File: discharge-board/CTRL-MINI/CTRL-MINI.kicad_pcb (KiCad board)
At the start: 2 copper layers, 119.4 x 71.1 mm, 17 parts, among them J1 Conn_01x04_Pin, J10 Conn_01x04_Pin, J11 MD2-L, J12 MD2-R, J13 Conn_01x08_Pin, J2 MD0-L, J3 MD0-R, J4 Screw_Terminal_01x02, J5 Conn_01x04_Pin, J6 MD1-L, J7 MD1-R, J8 RPP-L, J9 RPP-R, U1 BD50FC0FP

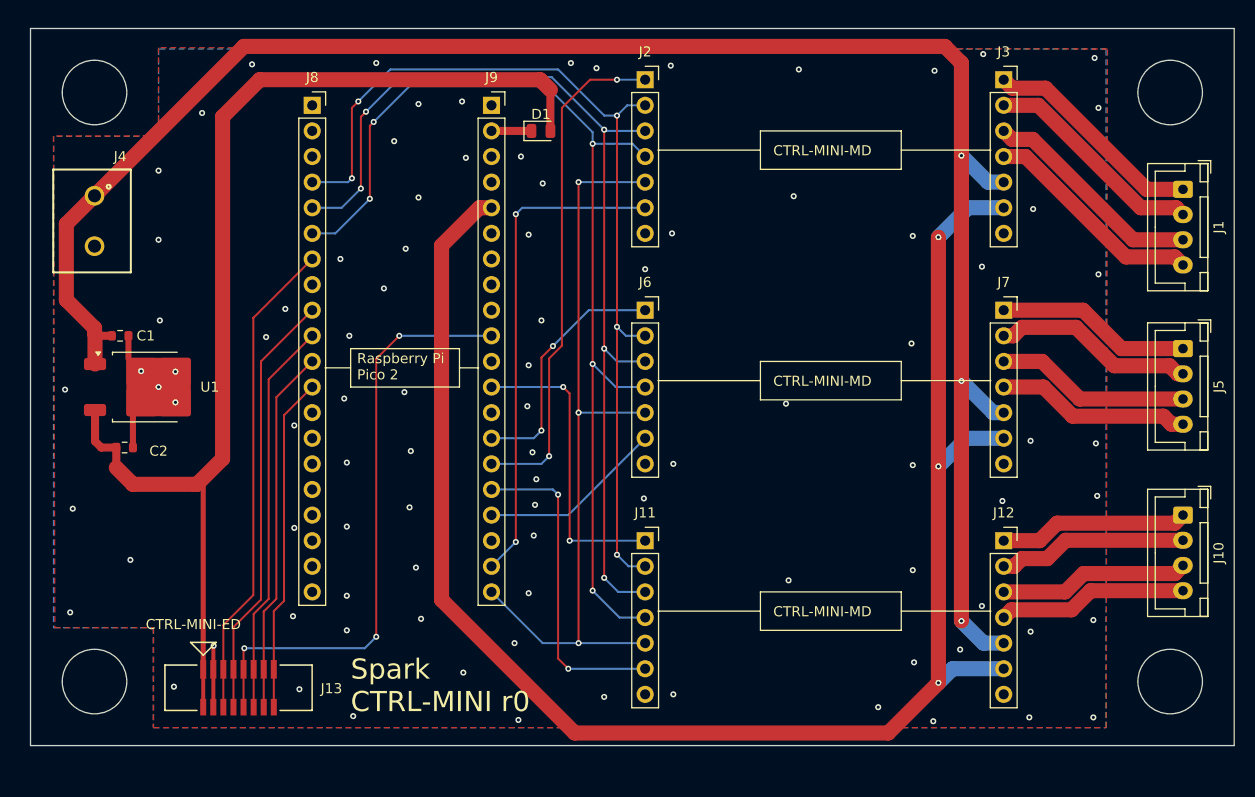
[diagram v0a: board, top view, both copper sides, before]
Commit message: Change CTRl-MINI MB size to metric
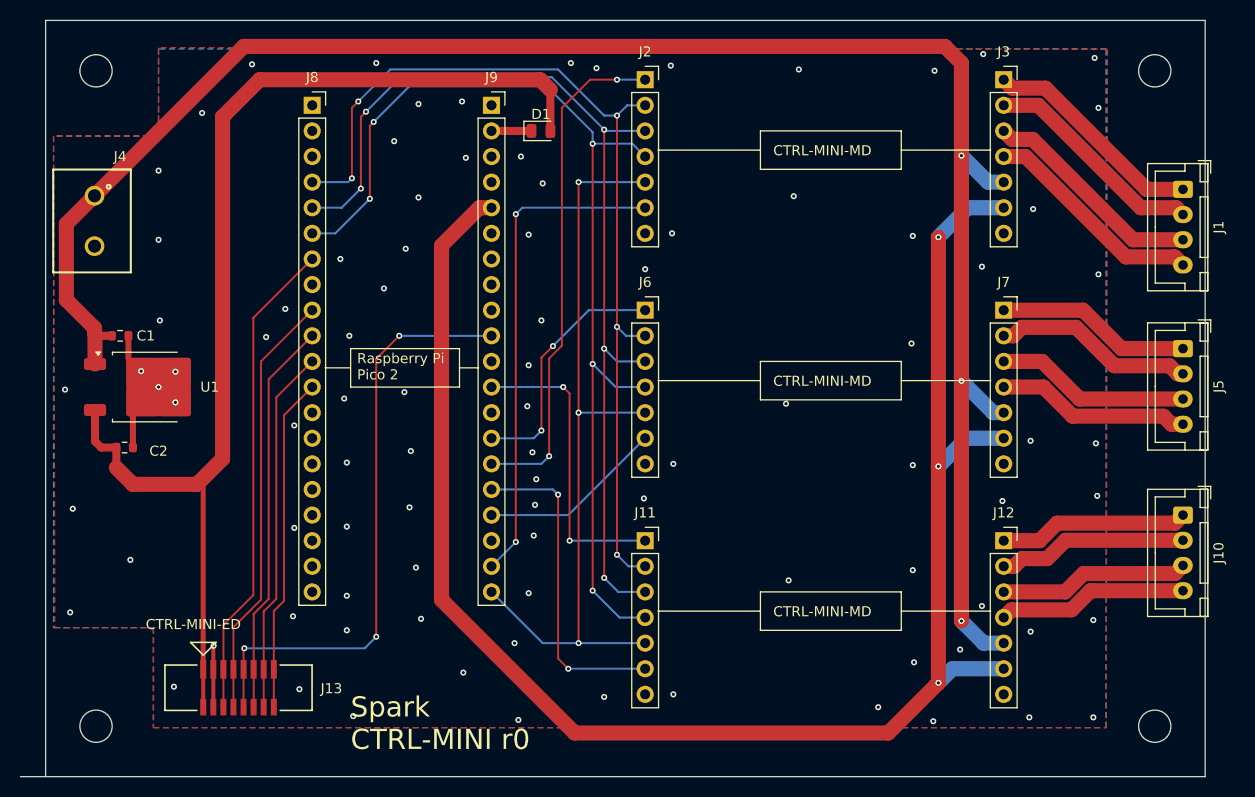
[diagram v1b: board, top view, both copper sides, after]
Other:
- board size 119.4 x 71.1 mm -> 117.5 x 75 mm

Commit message: Increase silkscreen width & avoid via-silk collision
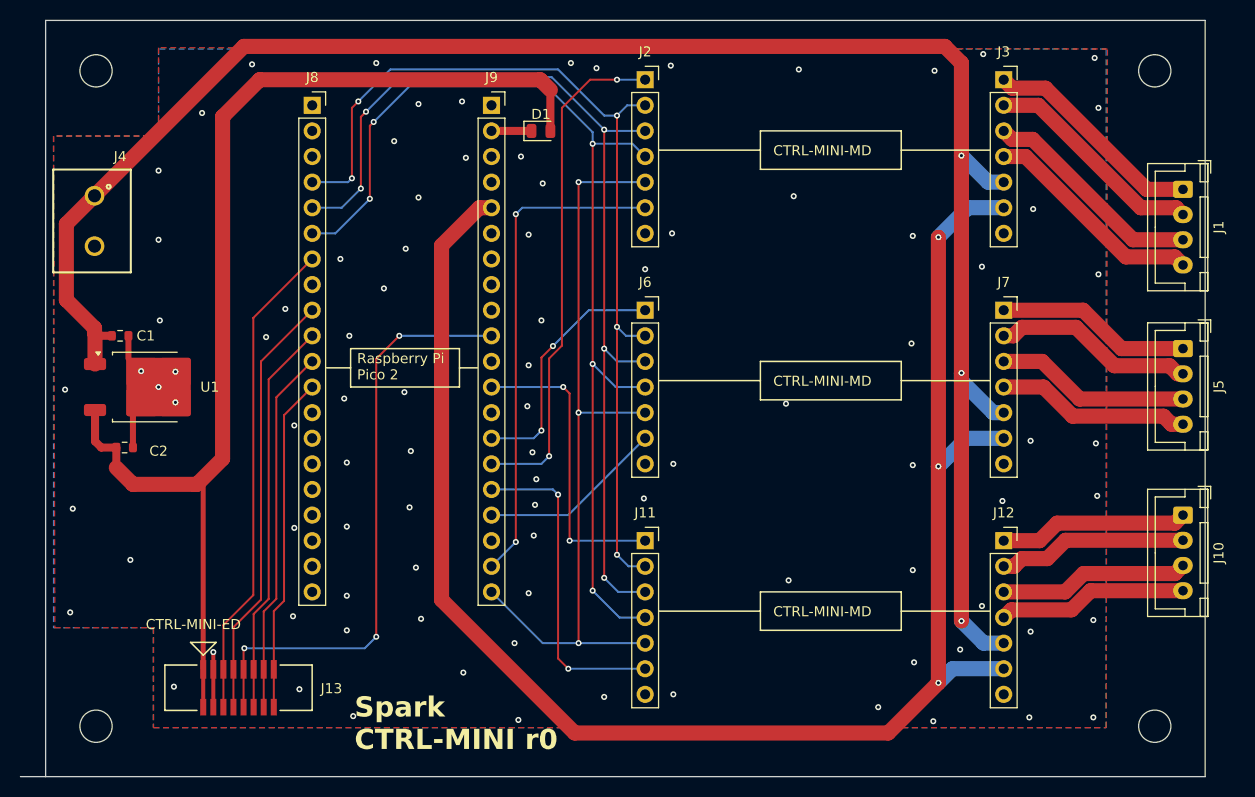
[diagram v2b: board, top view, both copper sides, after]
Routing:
- net +12V: track 184.8 -> 185.6 mm
- net GND: track 15.0 -> 14.4 mm
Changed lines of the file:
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@@
 	(gr_line
 		(start 106.045 84.455)
-		(end 107.95 84.455)
-		(stroke
-			(width 0.1)
+		(end 107.823 84.455)
+		(stroke
+			(width 0.15)
 			(type default)
 		)
@@
 	(gr_line
 		(start 149.86 108.585)
-		(end 158.75 108.585)
-		(stroke
-			(width 0.1)
+		(end 158.623 108.585)
+		(stroke
+			(width 0.15)
 			(type default)
 		)
@@
 		(end 149.86 106.68)
 		(stroke
-			(width 0.1)
+			(width 0.15)
 			(type default)
 		)
@@
 		(end 149.86 60.96)
 		(stroke
-			(width 0.1)
+			(width 0.15)
 			(type default)
 		)
@@
 		(end 135.89 110.49)
 		(stroke
-			(width 0.1)
+			(width 0.15)
 			(type default)
 		)
@@
 		(end 135.89 64.77)
 		(stroke
-			(width 0.1)
+			(width 0.15)
 			(type default)
 		)
@@
 	(gr_line
 		(start 135.89 85.725)
-		(end 125.73 85.725)
-		(stroke
-			(width 0.1)
+		(end 125.857 85.725)
+		(stroke
+			(width 0.15)
 			(type default)
 		)
@@
 		(end 135.89 60.96)
 		(stroke
-			(width 0.1)
+			(width 0.15)
 			(type default)
 		)
@@
 	(gr_line
 		(start 95.25 84.455)
-		(end 92.71 84.455)
-		(stroke
-			(width 0.1)
+		(end 92.837 84.455)
+		(stroke
+			(width 0.15)
 			(type default)
 		)
@@
 		(end 149.86 64.77)
 		(stroke
-			(width 0.1)
+			(width 0.15)
 			(type default)
 		)
@@
 	(gr_line
 		(start 135.89 62.865)
-		(end 125.73 62.865)
-		(stroke
-			(width 0.1)
+		(end 125.857 62.865)
+		(stroke
+			(width 0.15)
 			(type default)
 		)
@@
 		(end 149.86 83.82)
 		(stroke
-			(width 0.1)
+			(width 0.15)
 			(type default)
 		)
@@
 		(end 95.25 82.55)
 		(stroke
-			(width 0.1)
+			(width 0.15)
 			(type default)
 		)
@@
 		(end 149.86 110.49)
 		(stroke
-			(width 0.1)
+			(width 0.15)
 			(type default)
 		)
@@
 		(end 106.045 86.36)
 		(stroke
-			(width 0.1)
+			(width 0.15)
 			(type default)
 		)
@@
 		(end 135.89 87.63)
 		(stroke
-			(width 0.1)
+			(width 0.15)
 			(type default)
 		)
@@
 		(end 95.25 86.36)
 		(stroke
-			(width 0.1)
+			(width 0.15)
 			(type default)
 		)
@@
 		(end 135.89 83.82)
 		(stroke
-			(width 0.1)
+			(width 0.15)
 			(type default)
 		)
@@
 		(end 135.89 106.68)
 		(stroke
-			(width 0.1)
+			(width 0.15)
 			(type default)
 		)
@@
 		(end 149.86 87.63)
 		(stroke
-			(width 0.1)
+			(width 0.15)
 			(type default)
 		)
@@
 	(gr_line
 		(start 149.86 62.865)
-		(end 158.75 62.865)
-		(stroke
-			(width 0.1)
+		(end 158.623 62.865)
+		(stroke
+			(width 0.15)
 			(type default)
 		)
@@
 	(gr_line
 		(start 135.89 108.585)
-		(end 125.73 108.585)
-		(stroke
-			(width 0.1)
+		(end 125.857 108.585)
+		(stroke
+			(width 0.15)
 			(type default)
 		)
@@
 		(end 106.045 82.55)
 		(stroke
-			(width 0.1)
+			(width 0.15)
 			(type default)
 		)
@@
 	(gr_line
 		(start 149.86 85.725)
-		(end 158.75 85.725)
-		(stroke
-			(width 0.1)
+		(end 158.623 85.725)
+		(stroke
+			(width 0.15)
 			(type default)
 		)
@@
 			(font
 				(size 1 1)
-				(thickness 0.1)
+				(thickness 0.15)
 			)
 			(justify left bottom)
@@
 	)
 	(gr_text "Spark\nCTRL-MINI r0"
-		(at 95.25 122.5 0)
+		(at 95.631 122.5 0)
 		(layer "F.SilkS")
 		(effects
 			(font
 				(size 2 2)
-				(thickness 0.2)
+				(thickness 0.4)
+				(bold yes)
 			)
 			(justify left bottom)
@@
 			(font
 				(size 1 1)
-				(thickness 0.1)
+				(thickness 0.15)
 			)
 			(justify left bottom)
@@
 			(font
 				(size 1 1)
-				(thickness 0.1)
+				(thickness 0.15)
 			)
 			(justify left bottom)
@@
 			(font
 				(size 1 1)
-				(thickness 0.1)
+				(thickness 0.15)
 			)
 			(justify left bottom)
@@
 			(font
 				(size 1 1)
-				(thickness 0.1)
+				(thickness 0.15)
 			)
 			(justify left bottom)
@@
 	)
 	(segment
+		(start 81.63 112.649)
+		(end 81.63 114.36)
+		(width 0.4)
+		(layer "F.Cu")
+		(net 1)
+	)
+	(segment
 		(start 73.66 92.36)
 		(end 73.66 88.75)
@@
 	)
 	(segment
-		(start 81.661 112.014)
-		(end 81.63 112.045)
-		(width 0.4)
-		(layer "F.Cu")
-		(net 1)
-	)
-	(segment
 		(start 73.215 83.525)
 		(end 74.474 84.784)
@@
 		(net 1)
 	)
-	(segment
-		(start 81.63 112.045)
-		(end 81.63 114.36)
-		(width 0.4)
-		(layer "F.Cu")
-		(net 1)
-	)
 	(via
 		(at 100.584 86.868)
@@
 	)
 	(via
-		(at 81.661 112.014)
+		(at 81.63 112.649)
 		(size 0.6)
 		(drill 0.3)
@@
 	)
 	(segment
+		(start 155.829 84.963)
+		(end 155.829 63.406959)
+		(width 1.5)
+		(layer "F.Cu")
+		(net 2)
+	)
+	(segment
 		(start 67.056 70.184)
 		(end 67.056 77.724)
@@
 	(segment
 		(start 155.829 109.56704)
-		(end 155.829 85.758959)
+		(end 155.829 84.963)
 		(width 1.5)
 		(layer "F.Cu")
@@
 	)
 	(segment
-		(start 155.829 85.758959)
-		(end 155.829 63.406959)
-		(width 1.5)
-		(layer "F.Cu")
-		(net 2)
-	)
-	(segment
 		(start 69.85 67.39)
 		(end 67.056 70.184)
@@
 	)
 	(via
-		(at 155.829 85.758959)
+		(at 155.829 84.963)
 		(size 0.6)
 		(drill 0.3)
@@
 	(segment
 		(start 158.970041 88.9)
-		(end 155.829 85.758959)
-		(width 1.5)
-		(layer "B.Cu")
-		(net 2)
-	)
-	(segment
-		(start 160.02 88.9)
-		(end 158.970041 88.9)
+		(end 160.02 88.9)
 		(width 1.5)
 		(layer "B.Cu")
@@
 		(width 1.5)
 		(layer "B.Cu")
+		(net 2)
+	)
+	(segment
+		(start 155.829 84.963)
+		(end 155.829 85.758959)
+		(width 1.5)
+		(layer "B.Cu")
+		(net 2)
+	)
+	(segment
+		(start 155.829 85.758959)
+		(end 158.970041 88.9)
+		(width 1.5)
+		(layer "B.Cu")

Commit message: Improve manufacturability of MB, use SOD-523
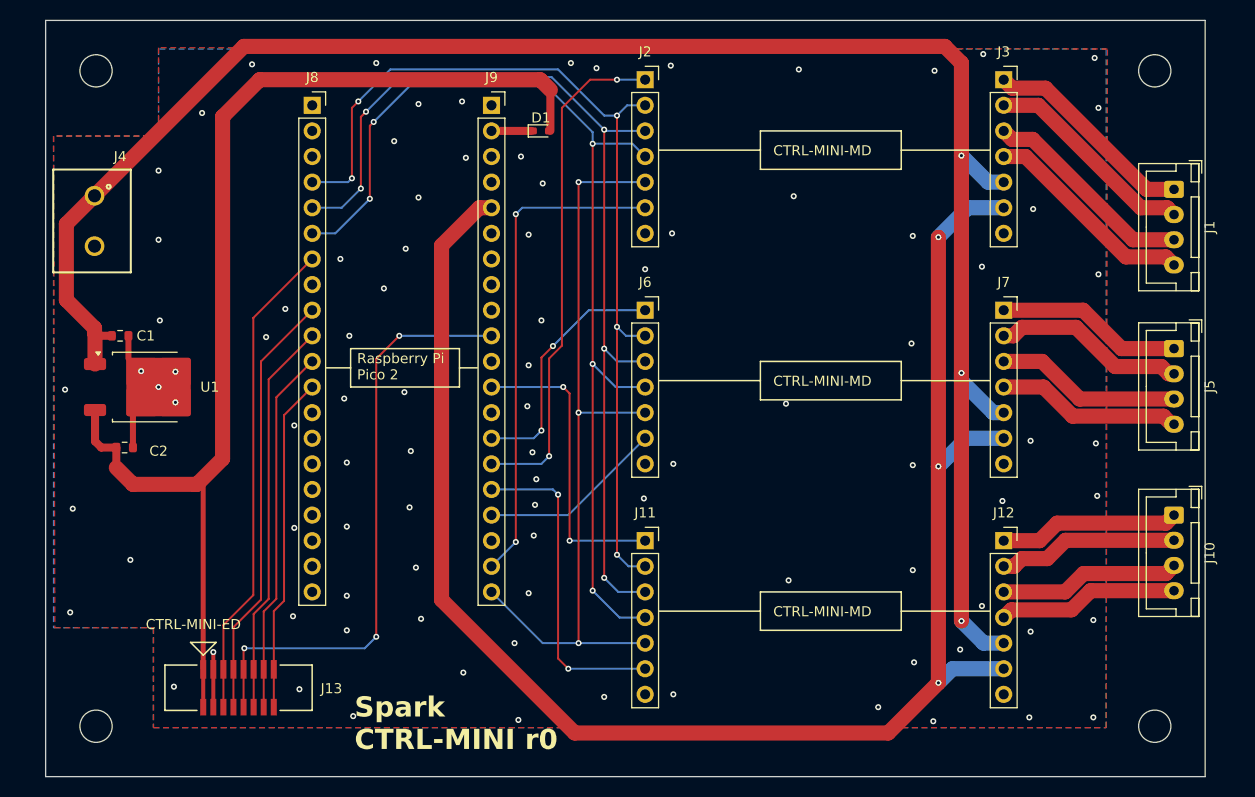
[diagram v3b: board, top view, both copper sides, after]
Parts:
- D1: footprint Diode_SMD:D_0805_2012Metric -> Diode_SMD:D_SOD-523
- moved J1 0.89 mm to (176.9, 66.8)
- moved J10 0.89 mm to (176.9, 99.1)
- moved J5 0.89 mm to (176.9, 82.5)
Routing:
- net Net-(J5-Pin_4): track 19.3 -> 18.2 mm
- net Net-(J5-Pin_3): track 19.3 -> 18.4 mm
- net Net-(J5-Pin_1): track 19.4 -> 18.5 mm
- net Net-(J10-Pin_4): track 18.9 -> 18.0 mm
- net Net-(J10-Pin_3): track 18.9 -> 18.0 mm
- net Net-(J10-Pin_2): track 18.8 -> 18.0 mm
- net Net-(J1-Pin_4): track 22.2 -> 21.3 mm
- net Net-(J1-Pin_3): track 22.3 -> 21.4 mm
- net Net-(J1-Pin_1): track 22.3 -> 21.4 mm
- net Net-(J10-Pin_1): track 18.8 -> 17.9 mm
- net Net-(J1-Pin_2): track 22.3 -> 21.4 mm
- net Net-(J5-Pin_2): track 20.0 -> 19.1 mm
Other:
- board size 117.5 x 75 mm -> 115 x 75 mm
